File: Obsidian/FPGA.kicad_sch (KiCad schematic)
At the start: 45 parts, among them Q1 BSS138LT1G, Q2 BSS138LT1G, SW2 SW_DIP_x01, U1 XC7A35T-CSG325, U28 24AA256UID-I_ST

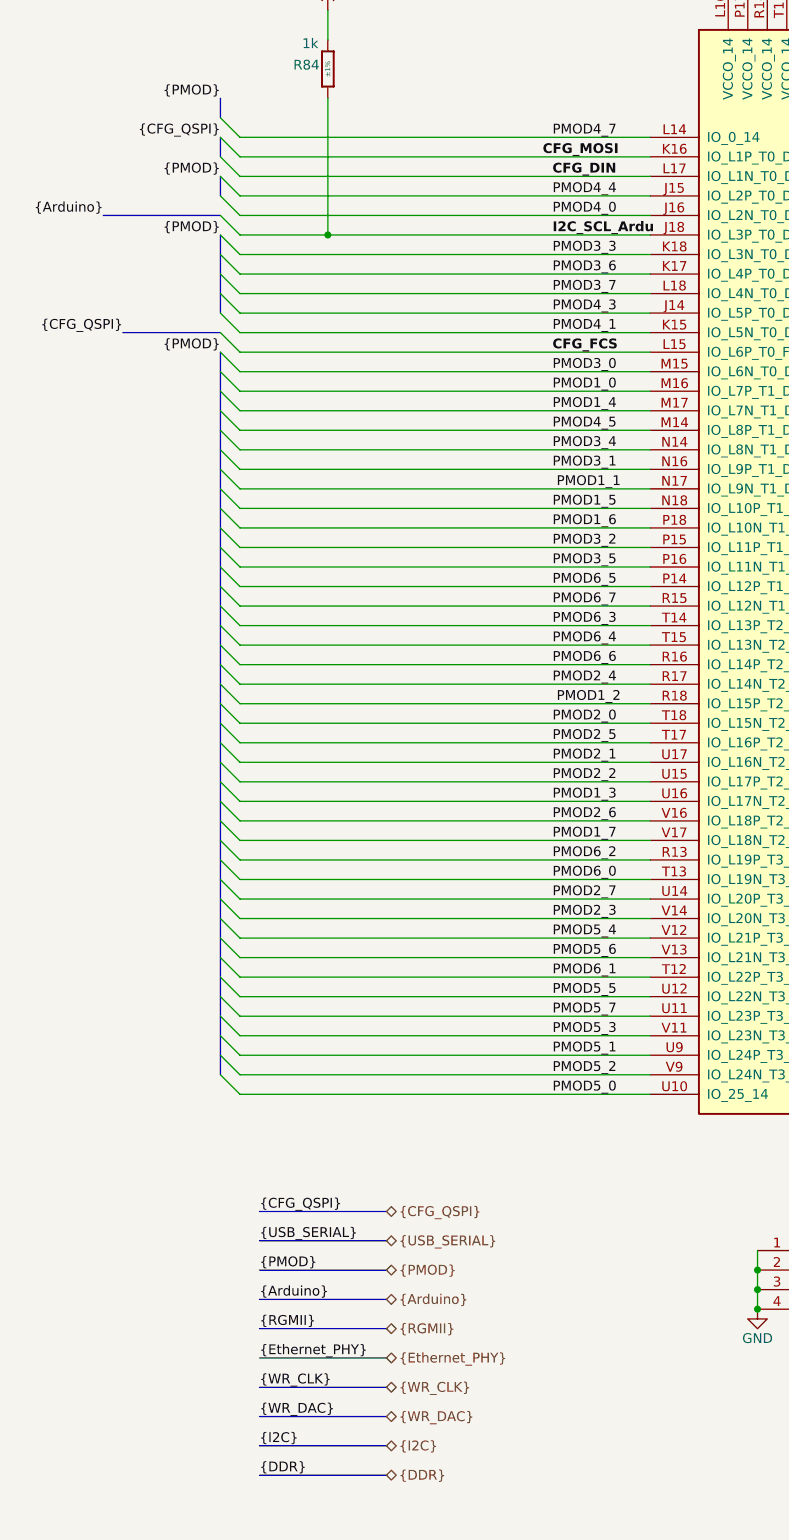
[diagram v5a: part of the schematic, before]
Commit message: adding flex connector
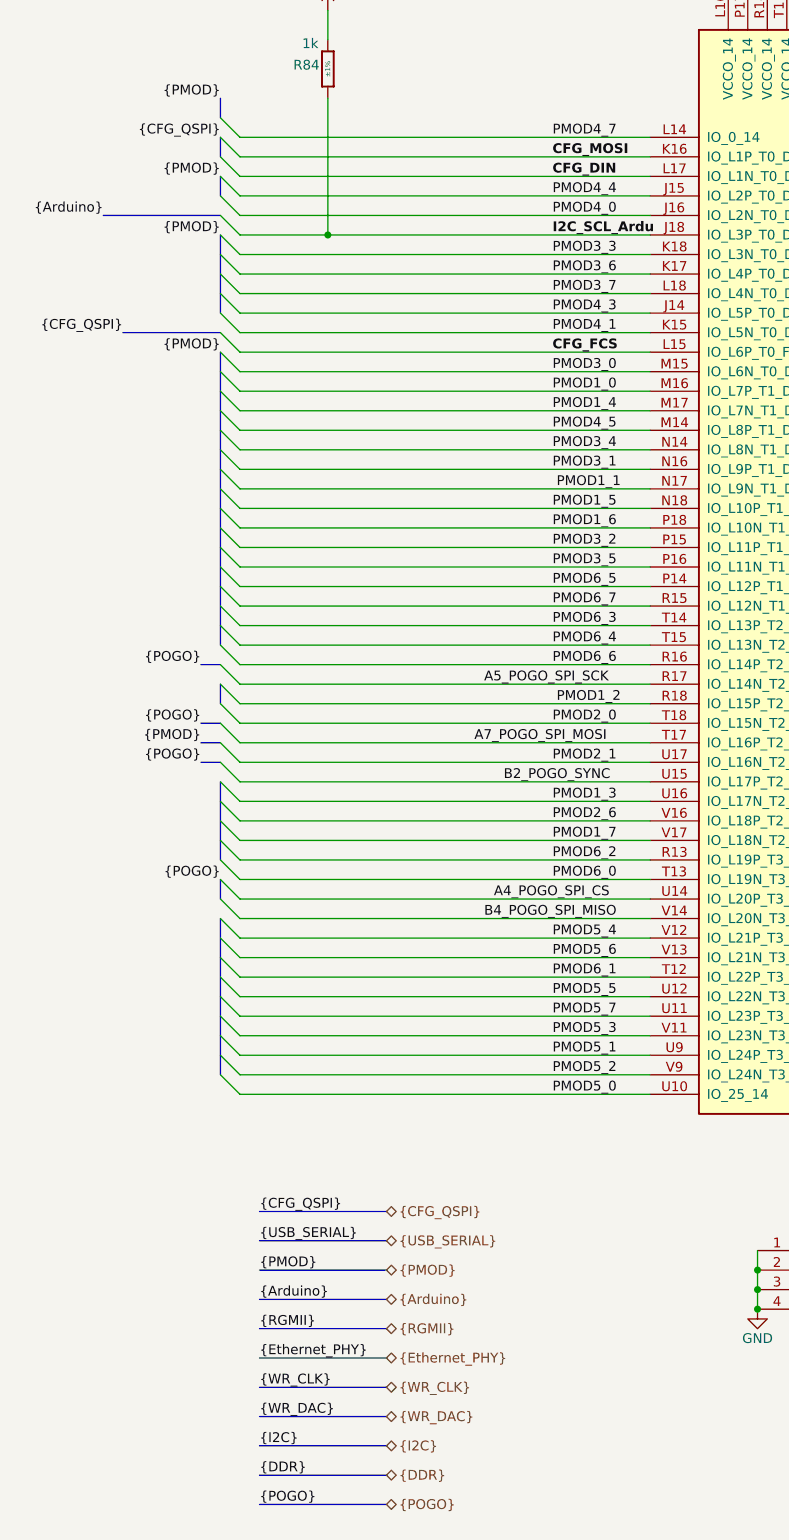
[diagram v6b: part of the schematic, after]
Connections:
- net PMOD2_2 renamed B2_POGO_SYNC
- net PMOD2_3 renamed B4_POGO_SPI_MISO
- net PMOD2_4 renamed A5_POGO_SPI_SCK
- net PMOD2_5 renamed A7_POGO_SPI_MOSI
- net PMOD2_7 renamed A4_POGO_SPI_CS

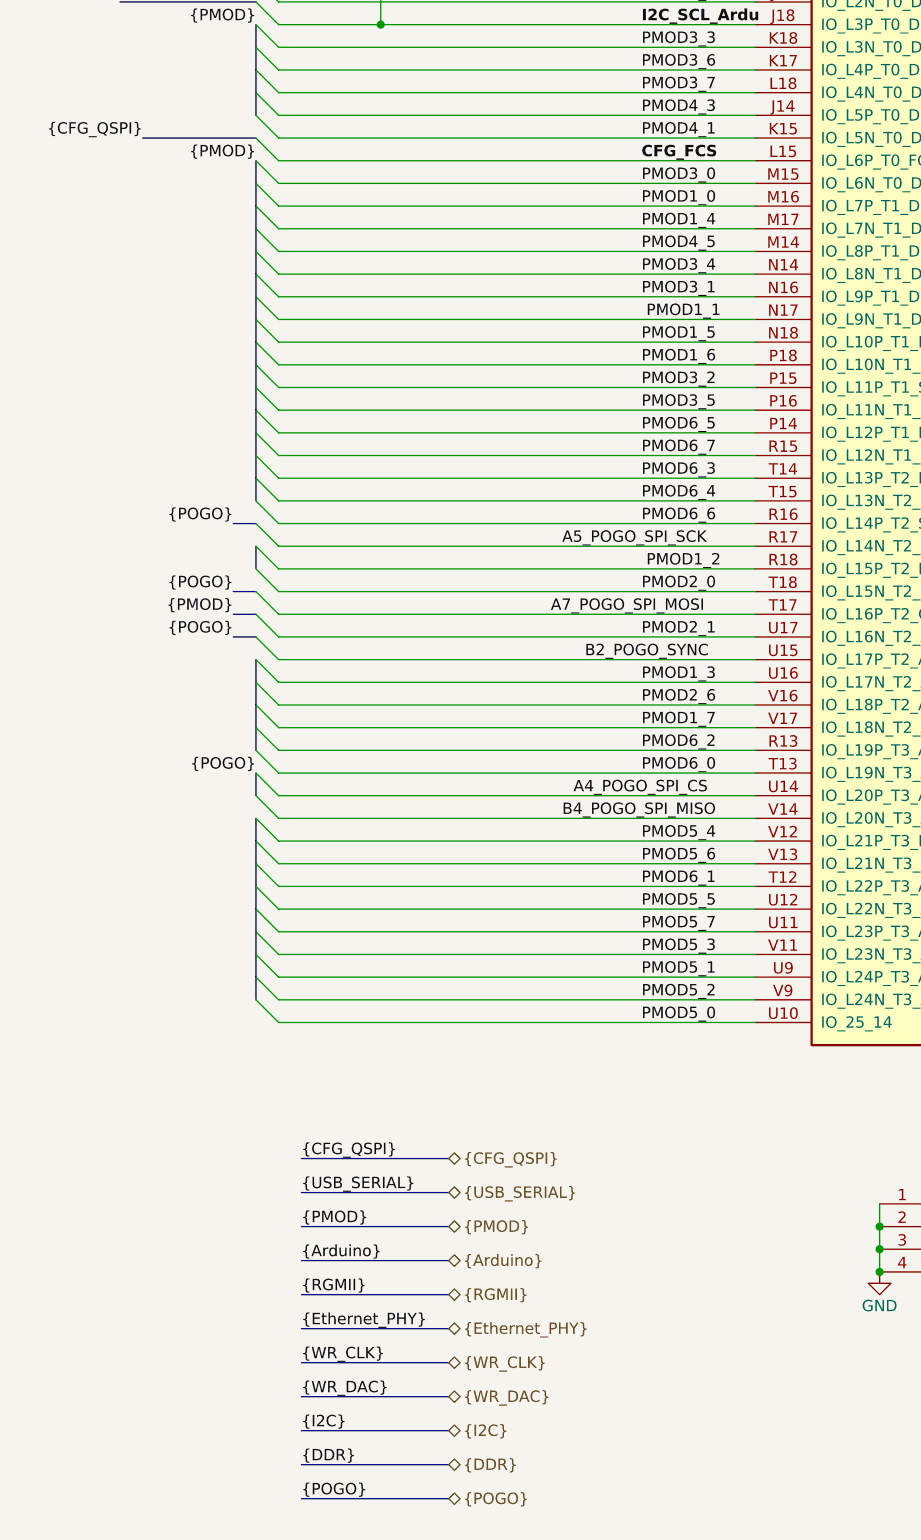
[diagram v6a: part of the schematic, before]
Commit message: Cleanup of the schematic
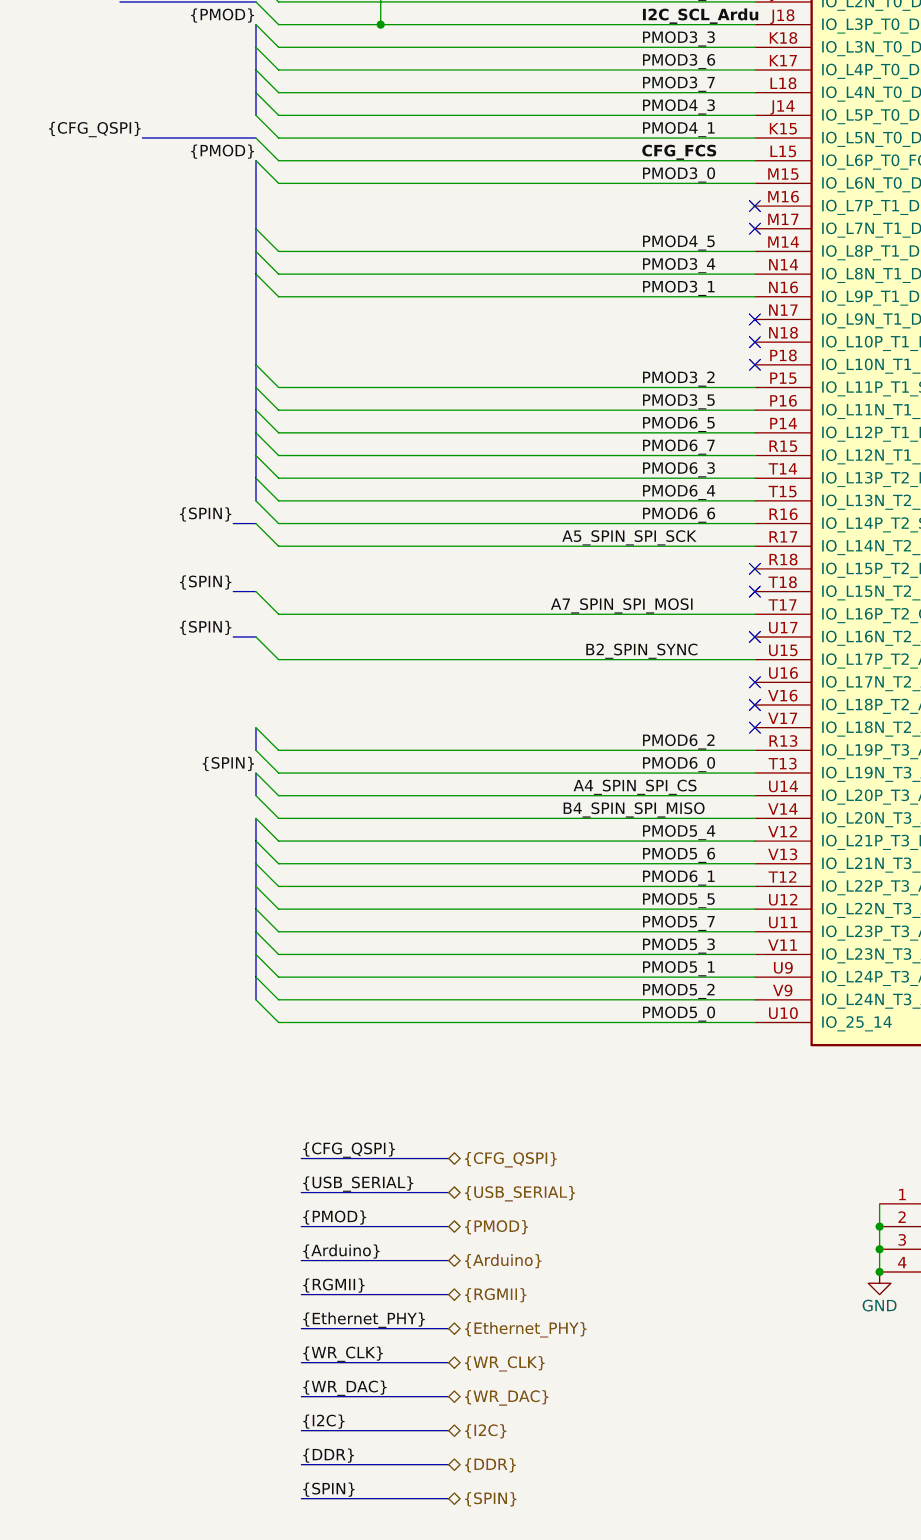
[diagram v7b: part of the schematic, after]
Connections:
- net A4_POGO_SPI_CS renamed A4_SPIN_SPI_CS
- net A5_POGO_SPI_SCK renamed A5_SPIN_SPI_SCK
- net A7_POGO_SPI_MOSI renamed A7_SPIN_SPI_MOSI
- net B2_POGO_SYNC renamed B2_SPIN_SYNC
- net B4_POGO_SPI_MISO renamed B4_SPIN_SPI_MISO
- net PMOD1_0: no longer names the net of U1.M16 (IO_L7P_T1_D09_14)
- net PMOD1_1: no longer names the net of U1.N17 (IO_L9N_T1_DQS_D13_14)
- net PMOD1_2: no longer names the net of U1.R18 (IO_L15P_T2_DQS_RDWR_B_14)
- net PMOD1_3: no longer names the net of U1.U16 (IO_L17N_T2_A13_D29_14)
- net PMOD1_4: no longer names the net of U1.M17 (IO_L7N_T1_D10_14)
- net PMOD1_5: no longer names the net of U1.N18 (IO_L10P_T1_D14_14)
- net PMOD1_6: no longer names the net of U1.P18 (IO_L10N_T1_D15_14)
- net PMOD1_7: no longer names the net of U1.V17 (IO_L18N_T2_A11_D27_14)
- net PMOD2_0: no longer names the net of U1.T18 (IO_L15N_T2_DQS_DOUT_CSO_B_14)
- net PMOD2_1: no longer names the net of U1.U17 (IO_L16N_T2_A15_D31_14)
- net PMOD2_6: no longer names the net of U1.V16 (IO_L18P_T2_A12_D28_14)
- no-connect marks 1 -> 12
